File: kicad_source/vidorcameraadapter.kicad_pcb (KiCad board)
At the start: 2 copper layers, 62 x 50 mm, 9 parts, among them CN1 CONN_02X26, CN2 CONN_02X10, CN3 CONN_01X03

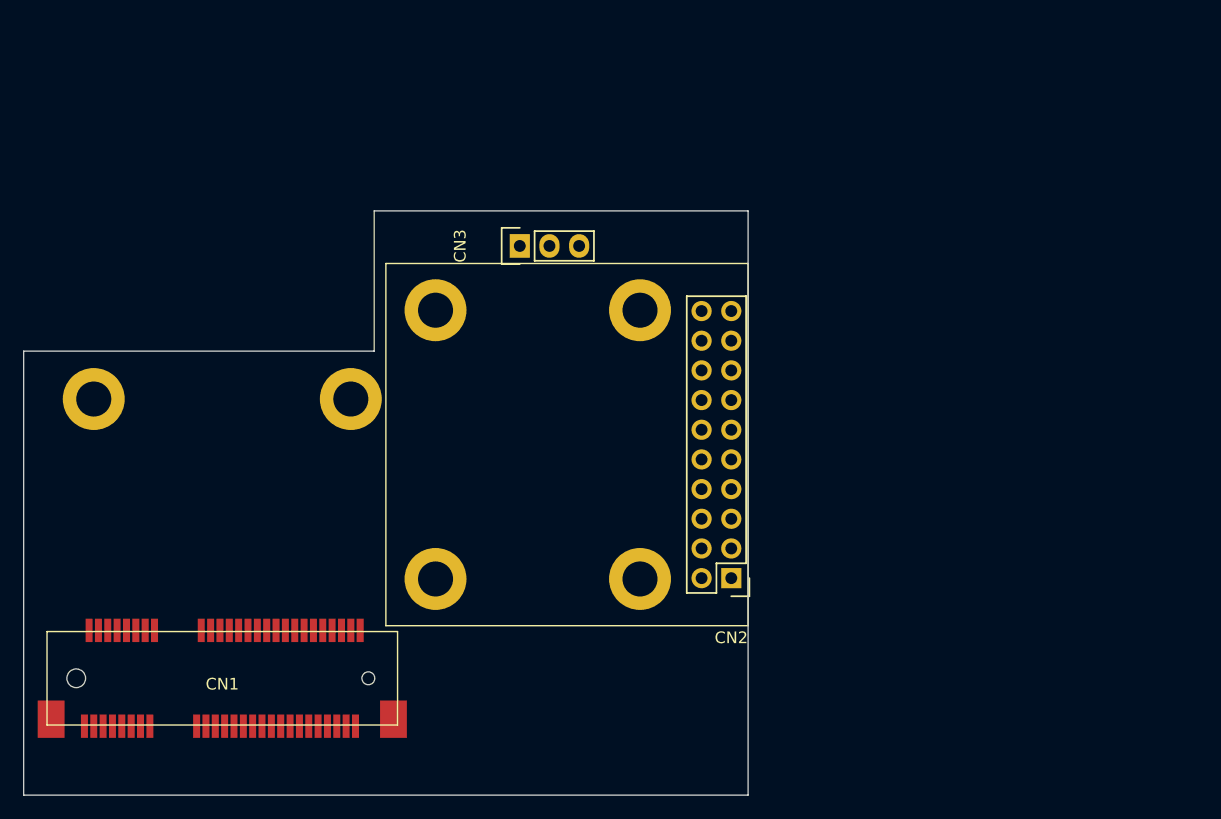
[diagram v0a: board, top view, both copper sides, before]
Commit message: corrected spacers, added resistors, made layout
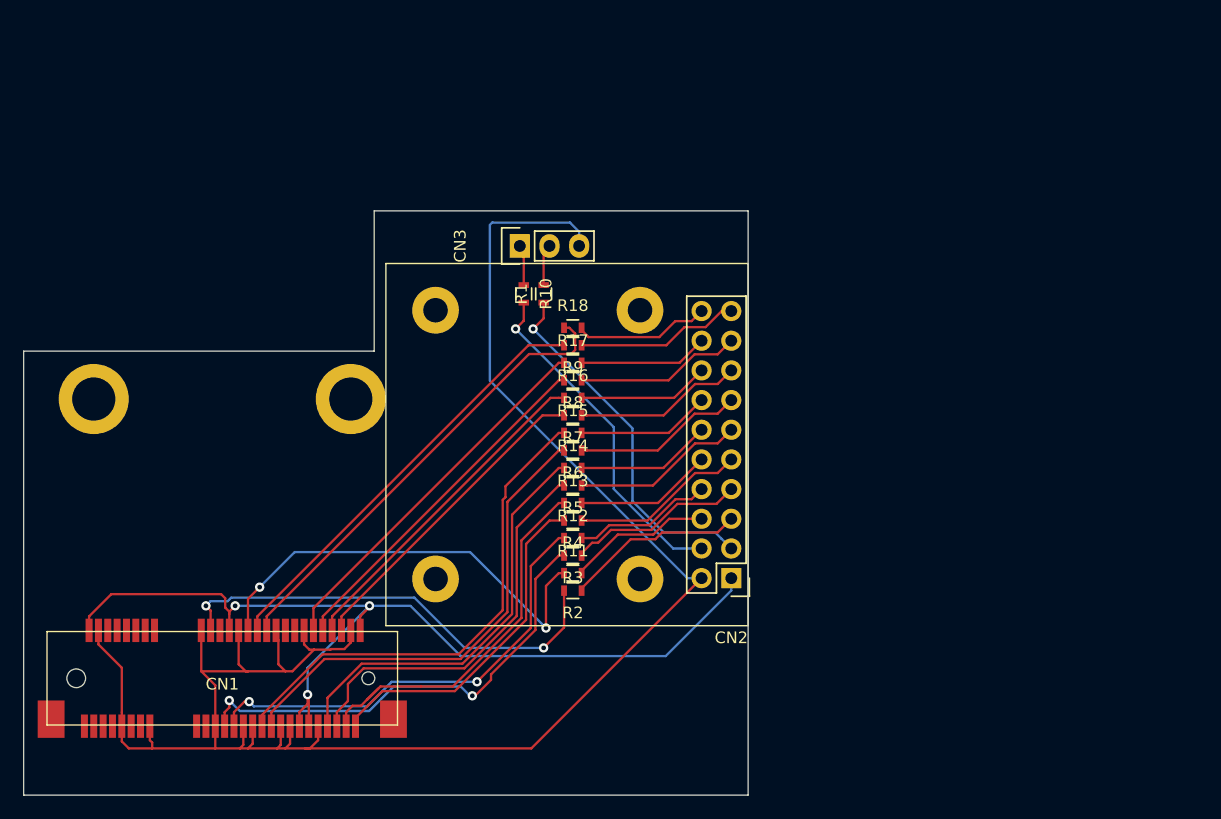
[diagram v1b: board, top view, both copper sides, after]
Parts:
- added R1: R_0603, resistors:R_0603, F.Cu at (122.5, 97.1)
- added R10: R_0603, resistors:R_0603, F.Cu at (120.8, 97.1)
- added R11: R_0603, resistors:R_0603, F.Cu at (125.0, 121.0)
- added R12: R_0603, resistors:R_0603, F.Cu at (125.0, 118.0)
- added R13: R_0603, resistors:R_0603, F.Cu at (125.0, 115.0)
- added R14: R_0603, resistors:R_0603, F.Cu at (125.0, 112.0)
- added R15: R_0603, resistors:R_0603, F.Cu at (125.0, 109.0)
- added R16: R_0603, resistors:R_0603, F.Cu at (125.0, 106.0)
- added R17: R_0603, resistors:R_0603, F.Cu at (125.0, 103.0)
- added R18: R_0603, resistors:R_0603, F.Cu at (125.0, 100.0)
- added R2: R_0603, resistors:R_0603, F.Cu at (125.0, 122.5)
- added R3: R_0603, resistors:R_0603, F.Cu at (125.0, 119.5)
- added R4: R_0603, resistors:R_0603, F.Cu at (125.0, 116.5)
- added R5: R_0603, resistors:R_0603, F.Cu at (125.0, 113.5)
- added R6: R_0603, resistors:R_0603, F.Cu at (125.0, 110.5)
- added R7: R_0603, resistors:R_0603, F.Cu at (125.0, 107.5)
- added R8: R_0603, resistors:R_0603, F.Cu at (125.0, 104.5)
- added R9: R_0603, resistors:R_0603, F.Cu at (125.0, 101.5)
- MECH1, MECH2: value WA-SMSI_9774010243 -> WA-SMSI_9774015151; footprint MECH_smd-spacer:WA-SMSI_9774010243 -> MECH_smd-spacer:WA-SMSI_9774015151
- MECH3, MECH4, MECH5, MECH6: value WA-SMSI_9774010243 -> WA-SMSI_97730606334; footprint MECH_smd-spacer:WA-SMSI_9774010243 -> MECH_smd-spacer:WA-SMSI_97730606334
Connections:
- CN1 pad 31: /DOUT9 -> /DOUT4
- CN1 pad 33: /DOUT8 -> /DOUT5
- CN1 pad 42: /DOUT7 -> /DOUT0
- CN1 pad 44: /DOUT5 -> /DOUT1
- CN1 pad 46: /DOUT3 -> /DOUT2
- CN1 pad 47: /DOUT4 -> /DOUT7
- CN1 pad 48: /DOUT1 -> /DOUT3
- CN1 pad 49: /DOUT2 -> /DOUT8
- CN1 pad 51: /DOUT0 -> /DOUT9
- CN2 pad 10: /DOUT8 -> /DOUT8_R
- CN2 pad 11: /DOUT7 -> /DOUT7_R
- CN2 pad 12: /DOUT6 -> /DOUT6_R
- CN2 pad 13: /DOUT5 -> /DOUT5_R
- CN2 pad 14: /DOUT4 -> /DOUT4_R
- CN2 pad 15: /DOUT3 -> /DOUT3_R
- CN2 pad 16: /DOUT2 -> /DOUT2_R
- CN2 pad 17: /DOUT1 -> /DOUT1_R
- CN2 pad 18: /DOUT0 -> /DOUT0_R
- CN2 pad 19: /RST -> /RST_R
- CN2 pad 20: /PWDN -> /PWDN_R
- CN2 pad 3: /SCL -> /SCL_R
- CN2 pad 4: /SDA -> /SDA_R
- CN2 pad 5: /VSYNC -> /VSYNC_R
- CN2 pad 6: /HREF -> /HREF_R
- CN2 pad 7: /PCLK -> /PCLK_R
- CN2 pad 8: /XCLK -> /XCLK_R
- CN2 pad 9: /DOUT9 -> /DOUT9_R
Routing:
- net GND: track 0.00 -> 162.2 mm
- net +3V3: track 0.00 -> 83.0 mm, vias 0 -> 3
- net /DOUT4: track 0.00 -> 42.9 mm
- net /DOUT5: track 0.00 -> 41.1 mm
- net /PCLK: track 0.00 -> 40.4 mm, vias 0 -> 2
- net /PWDN: track 0.00 -> 39.6 mm
- net /XCLK: track 0.00 -> 39.1 mm, vias 0 -> 2
- net /VSYNC: track 0.00 -> 38.9 mm, vias 0 -> 2
- net /HREF: track 0.00 -> 38.2 mm, vias 0 -> 2
- net /RST: track 0.00 -> 37.1 mm
- net /DOUT6: track 0.00 -> 35.8 mm
- net /DOUT7: track 0.00 -> 34.0 mm
- net /DOUT8: track 0.00 -> 32.5 mm
- net /DOUT0: track 0.00 -> 32.0 mm
- net /SCL_R: track 0.00 -> 31.0 mm, vias 0 -> 1
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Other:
- net class Default: trace_width 0.25 -> 0.2

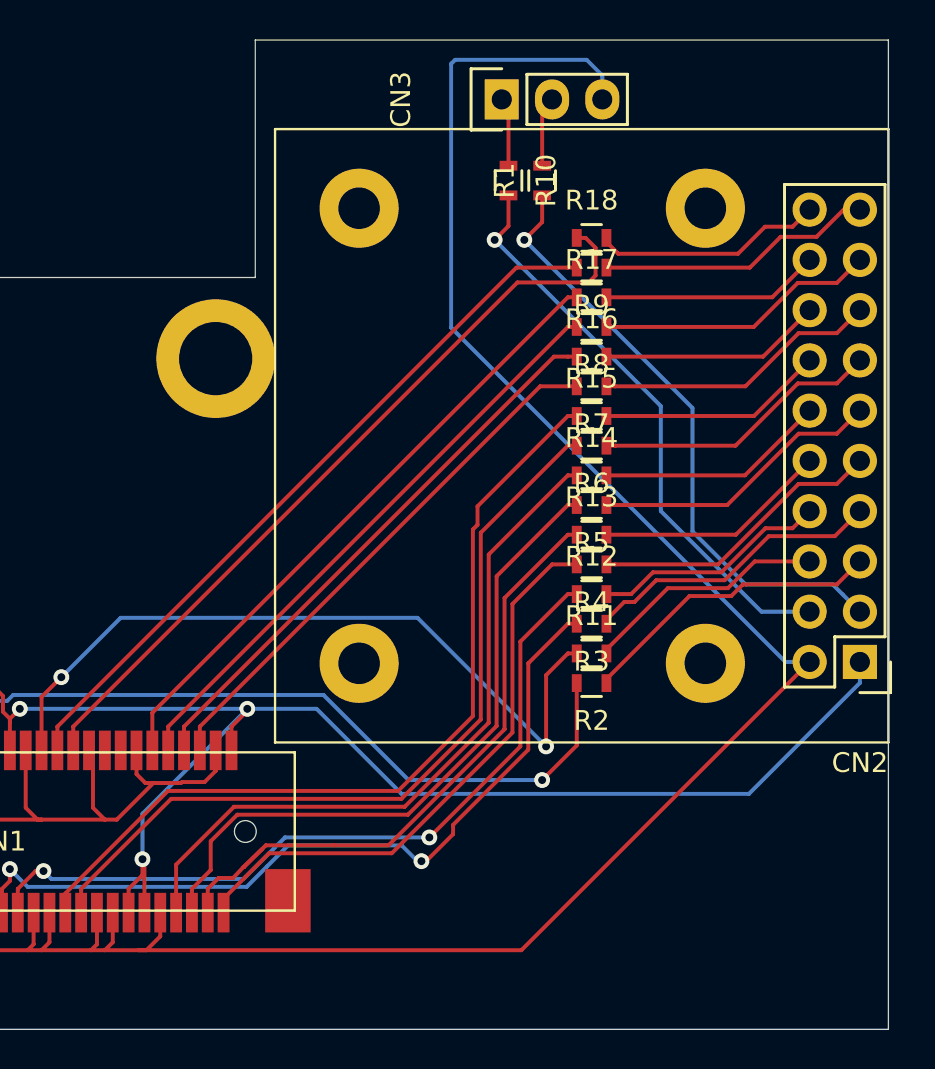
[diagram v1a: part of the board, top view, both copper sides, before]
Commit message: added 3d models, added mounting holes
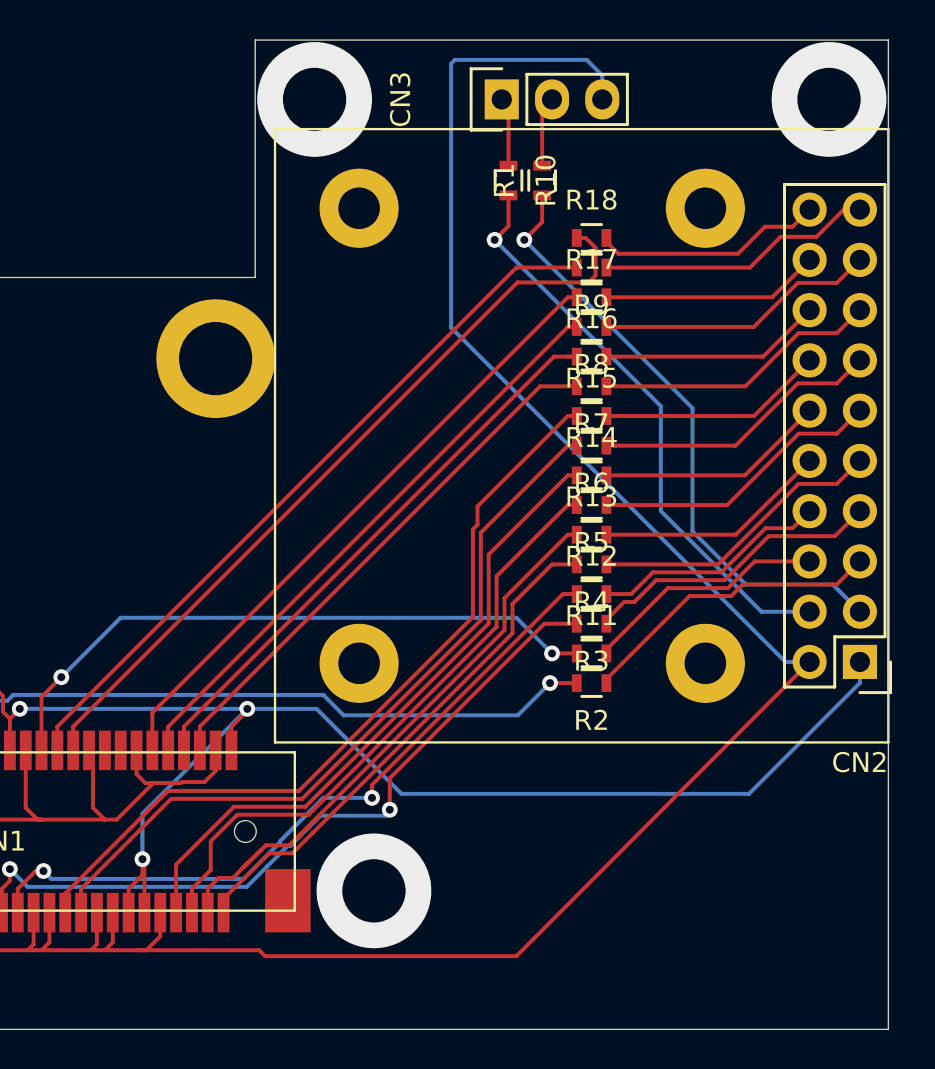
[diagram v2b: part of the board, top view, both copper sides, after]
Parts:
- CN2: footprint pin_headers:Pin_Header_Straight_2x10 -> CON_wuerth:WR-PHD_61302021821
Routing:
- net /HREF: track 38.2 -> 32.2 mm
- net /VSYNC: track 38.9 -> 34.3 mm
- net /DOUT8: track 32.5 -> 29.6 mm
- net /DOUT4: track 42.9 -> 39.9 mm
- net /DOUT7: track 34.0 -> 31.0 mm
- net /DOUT5: track 41.1 -> 38.1 mm
- net /DOUT6: track 35.8 -> 32.9 mm
- net /DOUT9: track 29.4 -> 26.4 mm
- net /XCLK: track 39.1 -> 36.4 mm
- net /PCLK: track 40.4 -> 37.9 mm
- net (no net): vias 0 -> 3

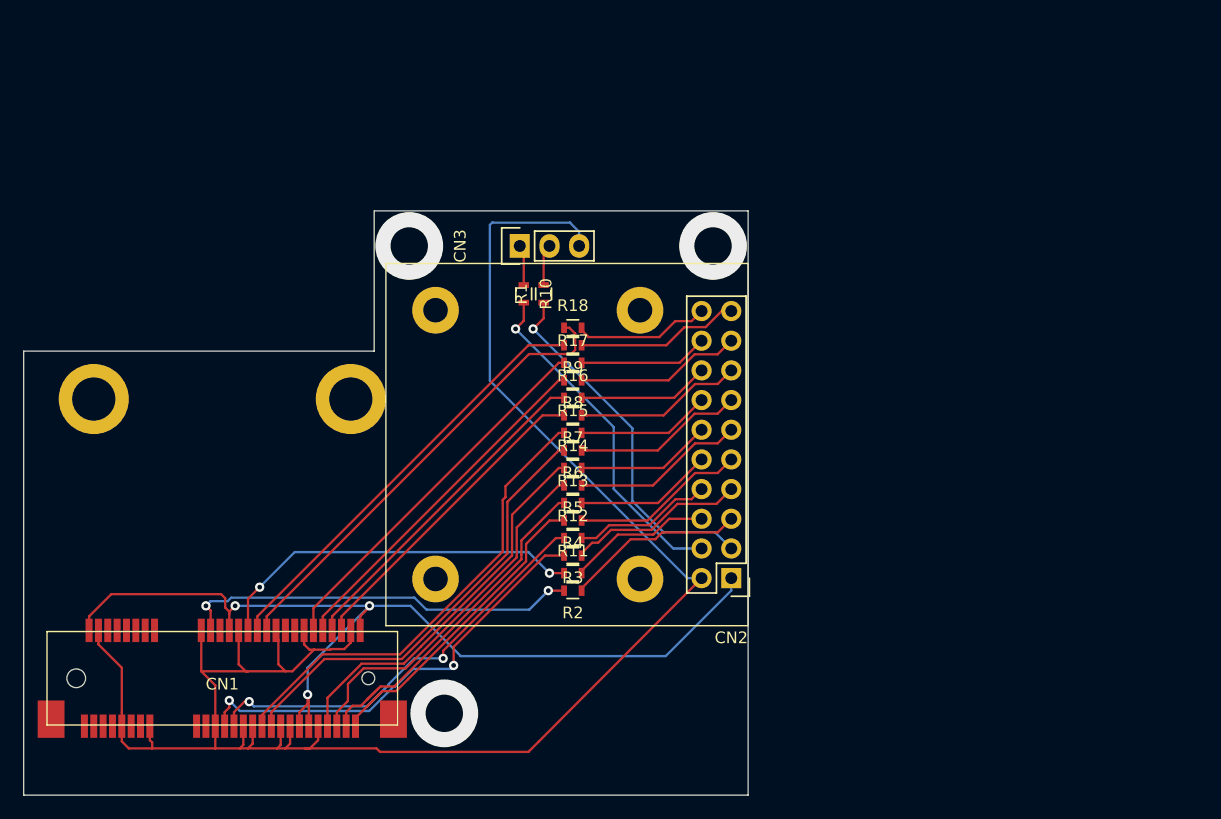
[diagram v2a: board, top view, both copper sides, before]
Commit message: added testpoints for all unused pins
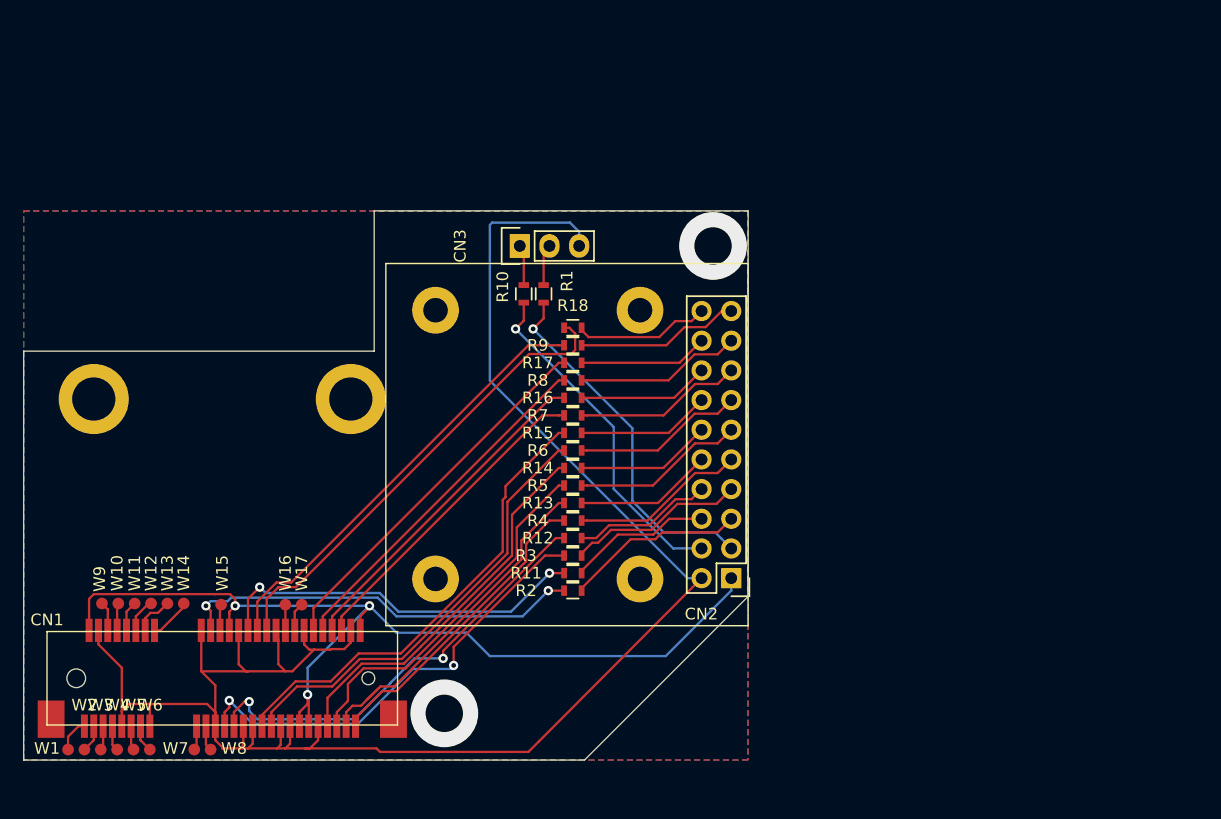
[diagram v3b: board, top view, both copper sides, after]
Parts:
- added W1: TEST_1P, wire_pads:SolderWirePad_single_1mmSMD, F.Cu at (81.8, 136.1)
- added W10: TEST_1P, wire_pads:SolderWirePad_single_1mmSMD, F.Cu at (86.1, 123.6)
- added W11: TEST_1P, wire_pads:SolderWirePad_single_1mmSMD, F.Cu at (87.5, 123.6)
- added W12: TEST_1P, wire_pads:SolderWirePad_single_1mmSMD, F.Cu at (88.9, 123.6)
- added W13: TEST_1P, wire_pads:SolderWirePad_single_1mmSMD, F.Cu at (90.3, 123.6)
- added W14: TEST_1P, wire_pads:SolderWirePad_single_1mmSMD, F.Cu at (91.7, 123.6)
- added W15: TEST_1P, wire_pads:SolderWirePad_single_1mmSMD, F.Cu at (94.9, 123.7)
- added W16: TEST_1P, wire_pads:SolderWirePad_single_1mmSMD, F.Cu at (100.4, 123.7)
- added W17: TEST_1P, wire_pads:SolderWirePad_single_1mmSMD, F.Cu at (101.8, 123.7)
- added W2: TEST_1P, wire_pads:SolderWirePad_single_1mmSMD, F.Cu at (83.2, 136.1)
- added W3: TEST_1P, wire_pads:SolderWirePad_single_1mmSMD, F.Cu at (84.6, 136.1)
- added W4: TEST_1P, wire_pads:SolderWirePad_single_1mmSMD, F.Cu at (86.0, 136.1)
- added W5: TEST_1P, wire_pads:SolderWirePad_single_1mmSMD, F.Cu at (87.4, 136.1)
- added W6: TEST_1P, wire_pads:SolderWirePad_single_1mmSMD, F.Cu at (88.8, 136.1)
- added W7: TEST_1P, wire_pads:SolderWirePad_single_1mmSMD, F.Cu at (92.6, 136.1)
- added W8: TEST_1P, wire_pads:SolderWirePad_single_1mmSMD, F.Cu at (94.0, 136.1)
- added W9: TEST_1P, wire_pads:SolderWirePad_single_1mmSMD, F.Cu at (84.7, 123.6)
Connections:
- CN1 pad 1: (no net) -> /RSVD0
- CN1 pad 10: (no net) -> /RSVD6
- CN1 pad 11: (no net) -> /RSVD7
- CN1 pad 12: (no net) -> /RSVD8
- CN1 pad 13: (no net) -> /RSVD9
- CN1 pad 14: (no net) -> /RSVD10
- CN1 pad 16: (no net) -> /RSVD11
- CN1 pad 17: (no net) -> /RSVD12
- CN1 pad 19: (no net) -> /RSVD13
- CN1 pad 22: (no net) -> /PEX_RST
- CN1 pad 3: (no net) -> /RSVD1
- CN1 pad 36: (no net) -> /USB_DM
- CN1 pad 38: (no net) -> /USB_DP
- CN1 pad 5: (no net) -> /RSVD2
- CN1 pad 6: (no net) -> /RSVD3
- CN1 pad 7: (no net) -> /RSVD4
- CN1 pad 8: (no net) -> /RSVD5
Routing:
- net /RSVD11: track 0.00 -> 3.63 mm
- net /RSVD10: track 0.00 -> 3.46 mm
- net /RSVD8: track 0.00 -> 2.96 mm
- net /RSVD0: track 0.00 -> 2.87 mm
- net /RSVD6: track 0.00 -> 2.59 mm
- net /RSVD3: track 0.00 -> 2.51 mm
- net /USB_DP: track 0.00 -> 2.45 mm
- net /RSVD5: track 0.00 -> 2.34 mm
- net /RSVD9: track 0.00 -> 2.33 mm
- net /RSVD1: track 0.00 -> 2.33 mm
- net /PEX_RST: track 0.00 -> 2.24 mm
- net /USB_DM: track 0.00 -> 2.20 mm
- net /RSVD4: track 0.00 -> 2.17 mm
- net /RSVD13: track 0.00 -> 2.17 mm
- net /RSVD7: track 0.00 -> 2.08 mm
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- added copper zone on B.Cu, net GND
- added copper zone on F.Cu, net GND
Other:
- board size 62 x 50 mm -> 62 x 47 mm

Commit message: updated layout, made edge smoother, generated pdf schematic and images
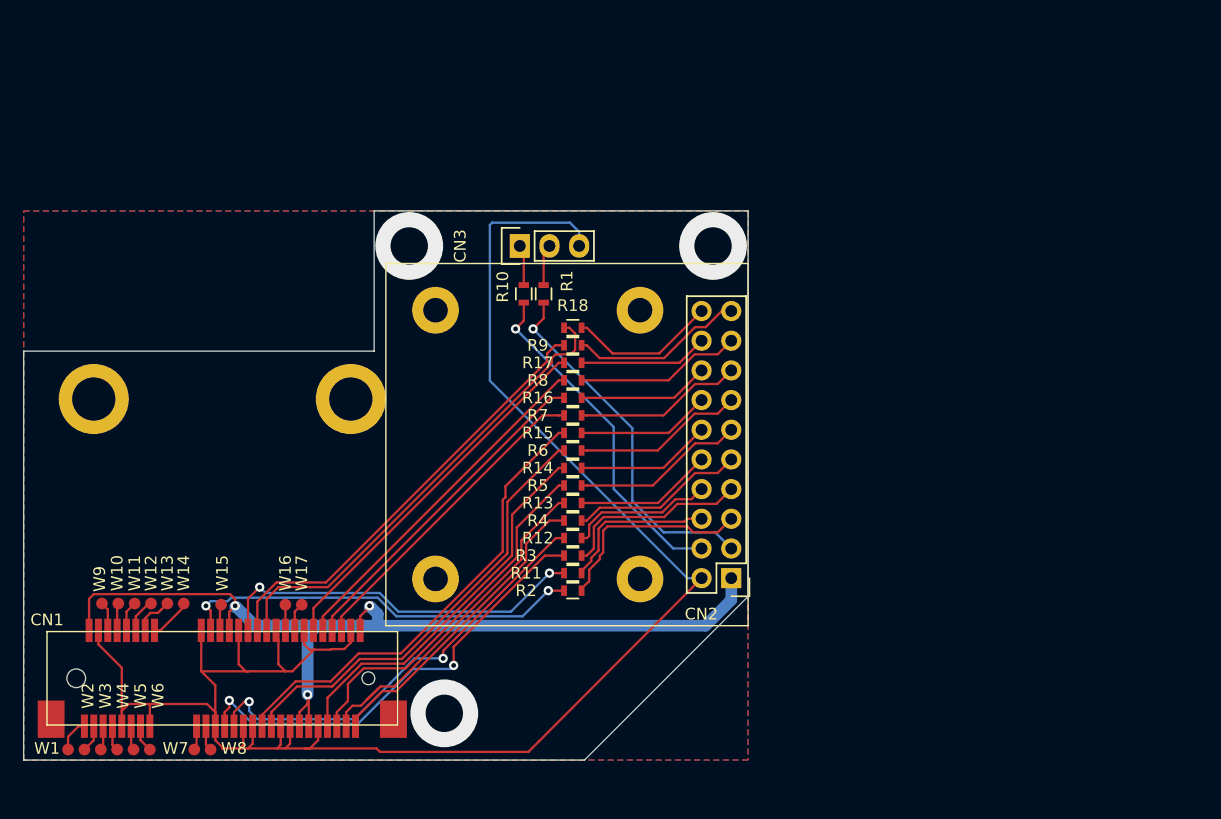
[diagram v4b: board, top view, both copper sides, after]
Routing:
- net +3V3: track 84.0 -> 80.7 mm
- net /VSYNC_R: track 15.5 -> 17.7 mm
- net /HREF_R: track 12.3 -> 13.6 mm
- net /PWDN_R: track 11.6 -> 12.7 mm
- net /PCLK_R: track 15.3 -> 16.3 mm
- net /RST_R: track 14.0 -> 14.9 mm
- net /XCLK_R: track 12.0 -> 12.6 mm
- net (no net): vias 2 -> 3
